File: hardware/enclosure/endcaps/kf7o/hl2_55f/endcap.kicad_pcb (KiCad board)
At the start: 2 copper layers, 106 x 55 mm, 22 parts, among them U1 IS31AP4996

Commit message: Build9 final changes before submission
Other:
- board text added: "11-16V"
- board text added: "11-16V 2A"
- board text removed: "11-18V"
- board text removed: "11-18V 2A"
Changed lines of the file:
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@@
     (effects (font (size 2 2) (thickness 0.3)))
   )
-  (gr_text 11-18V (at 59.9 83.9) (layer Eco1.User)
+  (gr_text 11-16V (at 59.9 83.9) (layer Eco1.User)
     (effects (font (size 2 2) (thickness 0.3)))
   )
@@
     (effects (font (size 2.5 2.5) (thickness 0.3)))
   )
-  (gr_text "11-18V\n2A" (at 60.2 86.2 270) (layer F.SilkS)
+  (gr_text "11-16V\n2A" (at 60.2 86.2 270) (layer F.SilkS)
     (effects (font (size 2.5 2.5) (thickness 0.3)) (justify right))
   )

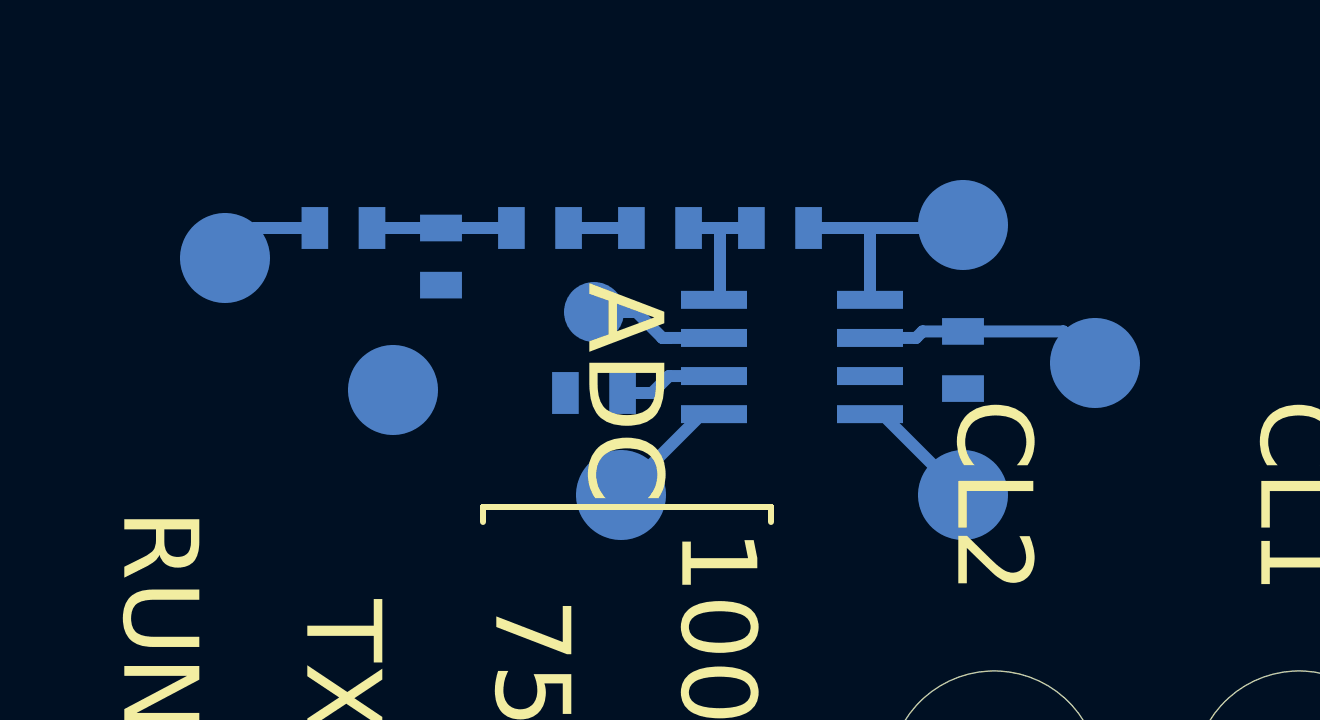
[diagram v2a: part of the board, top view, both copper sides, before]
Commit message: Add LPF for fan on latest end plates
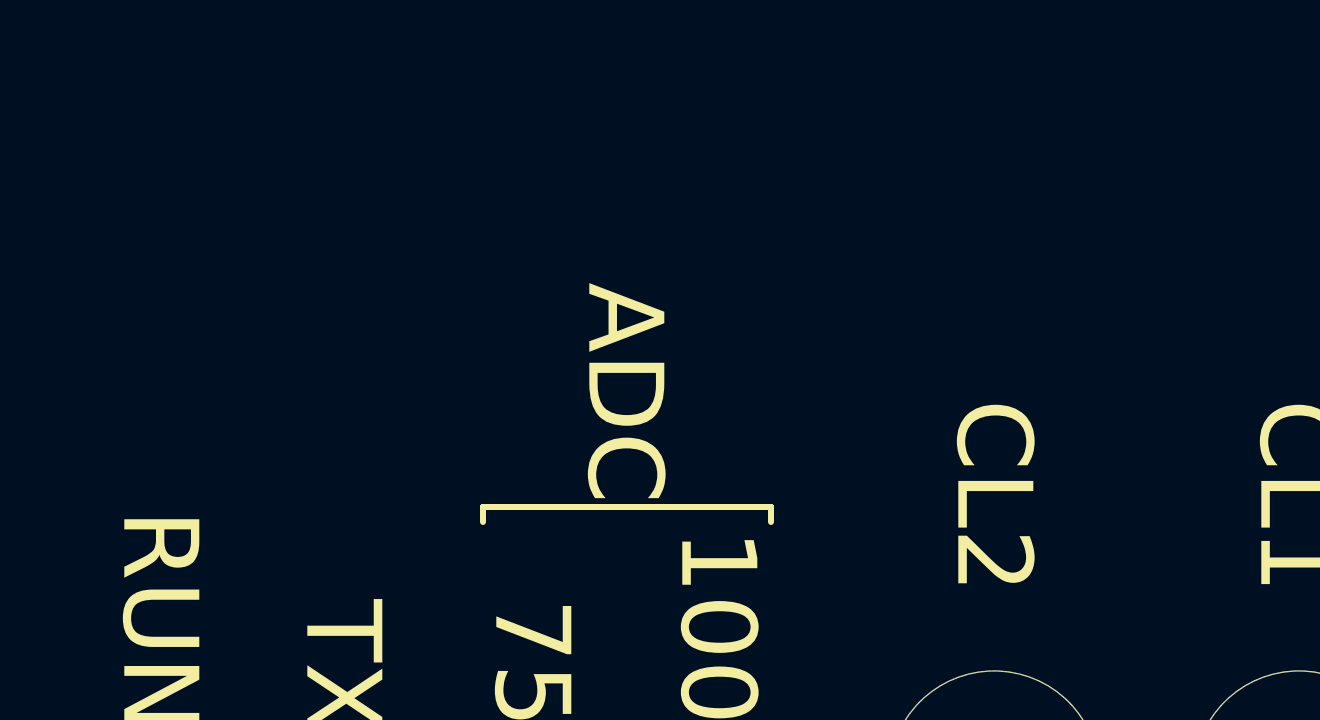
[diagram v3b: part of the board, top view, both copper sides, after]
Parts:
- removed C1, C4: 1uF, endcaplib:SMD-0805
- removed C2: 0.1uF, endcaplib:SMD-0805
- removed C3: 0.47uF, endcaplib:SMD-0805
- removed R1: 220, endcaplib:SMD-0805
- removed R2, R3: 20K, endcaplib:SMD-0805
- removed TP1: PWM, TestPoint:TestPoint_Pad_D3.0mm
- removed TP2: GND, TestPoint:TestPoint_Pad_D3.0mm
- removed TP3: 3.3V, TestPoint:TestPoint_Pad_D3.0mm
- removed TP4: A+, TestPoint:TestPoint_Pad_D3.0mm
- removed TP5: A-, TestPoint:TestPoint_Pad_D3.0mm
- removed TP6: SD, TestPoint:TestPoint_Pad_D3.0mm
- removed TP7: IN+, TestPoint:TestPoint_Pad_D2.0mm
- removed U1: IS31AP4996, endcaplib:SOIC-8
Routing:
- net Net-(C4-Pad2): track 8.03 -> 0.00 mm
- net Net-(R3-Pad1): track 7.58 -> 0.00 mm
- net Net-(C1-Pad1): track 4.65 -> 0.00 mm
- net Net-(R2-Pad1): track 4.57 -> 0.00 mm
- net Net-(TP7-Pad1): track 4.36 -> 0.00 mm
- net Net-(TP4-Pad1): track 4.22 -> 0.00 mm
- net Net-(TP6-Pad1): track 4.22 -> 0.00 mm
- net Net-(R1-Pad2): track 3.41 -> 0.00 mm
- net Net-(C3-Pad1): track 3.28 -> 0.00 mm
- net Net-(C2-Pad1): track 2.09 -> 0.00 mm
